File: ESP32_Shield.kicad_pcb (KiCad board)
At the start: 4 copper layers, 69 x 40.6 mm, 36 parts, among them J1 BME280, SHT40 Module, J10 SCD40 Module, J11 Conn_01x03, J12 Conn_01x03, J13 SCD40 Module, J14 BME280, SHT40 Module, J2 SCD40 Module, J3 Conn_01x02, J4 Qwiic_Vertical, J5 Conn_01x02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

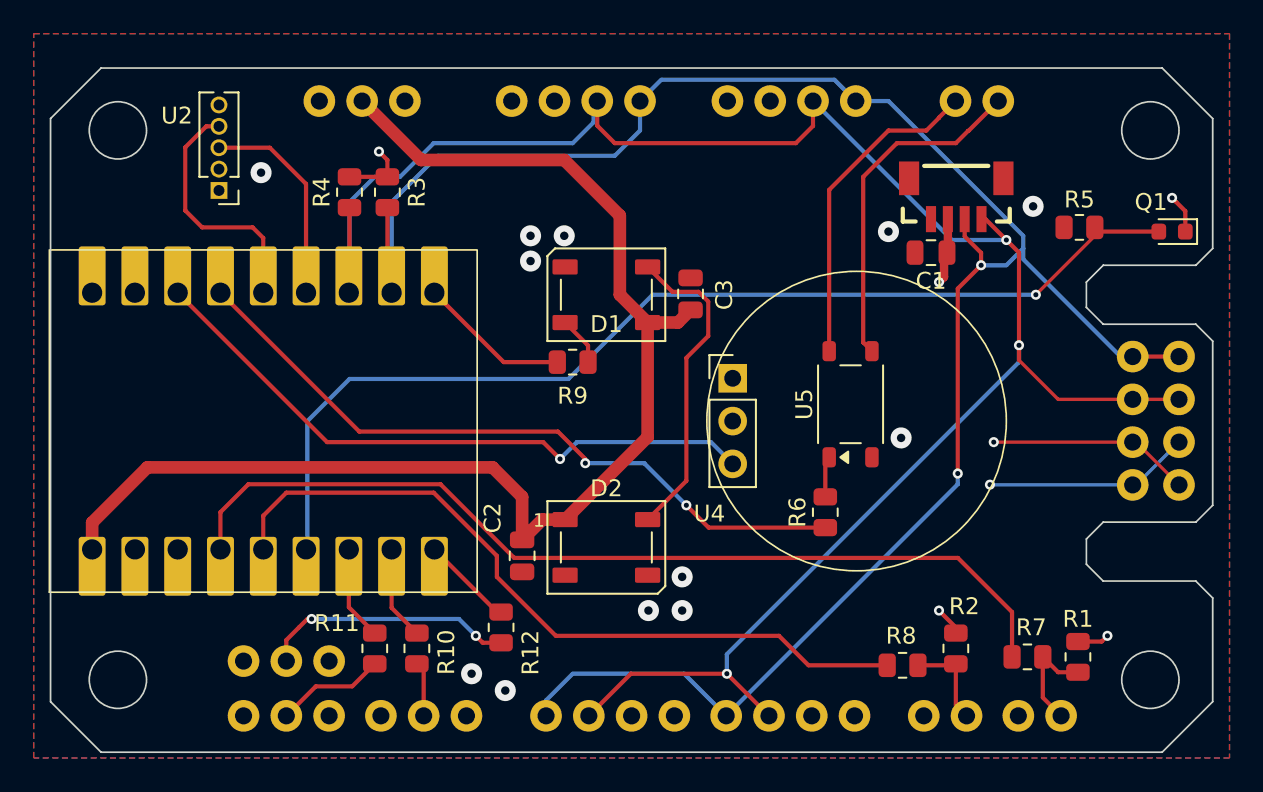
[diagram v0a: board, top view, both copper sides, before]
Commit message: Feature/description on soldermask (#2)
* fix Readme

* enhance README with KiBOT usage instructions and asset generation workflow

* make shure everithing is english

* improve readme

* fix upload path

* fix tittle in readme

* add silk screen and mmWave connector

* Update artifact name in fabrication workflow

* try other pr pipeline

* add more JST connectors for UART

* add jst connector for aditional gpios
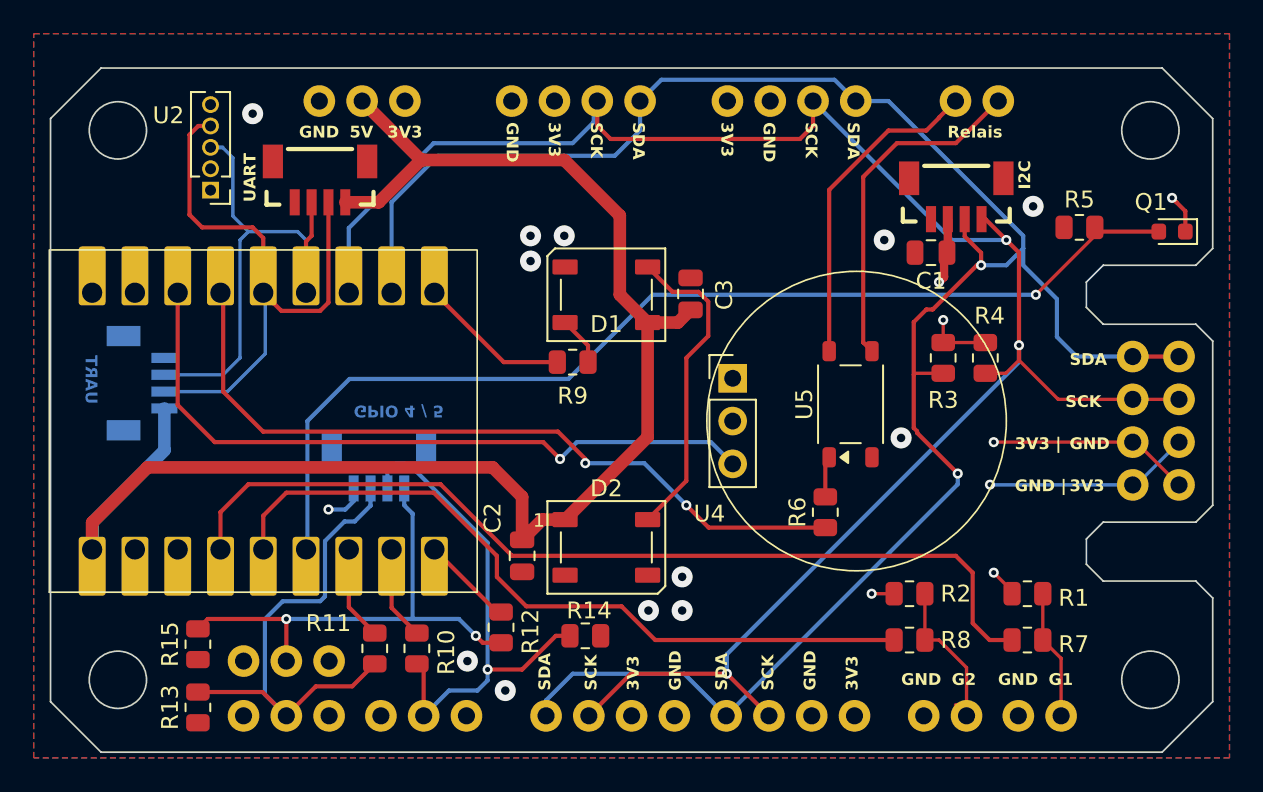
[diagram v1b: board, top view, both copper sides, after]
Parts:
- added J15: mmWave Connector, PCM_SparkFun-Connector:JST_1x04_P1.0mm_Vertical_SMD, B.Cu at (96.2, 86.2)
- added J16: mmWave Connector, PCM_SparkFun-Connector:JST_1x04_P1.0mm_Vertical_SMD, F.Cu at (107.0, 74.0)
- added J17: mmWave Connector, PCM_SparkFun-Connector:JST_1x04_P1.0mm_Vertical_SMD, B.Cu at (110.5, 91.0)
- added R13: 2k2, Resistor_SMD:R_0805_2012Metric, F.Cu at (99.8, 105.5)
- added R14: 2k2, Resistor_SMD:R_0805_2012Metric, F.Cu at (122.8, 101.2)
- added R15: 2k2, Resistor_SMD:R_0805_2012Metric, F.Cu at (99.8, 101.8)
- moved R4 39.0 mm to (146.5, 84.8)
- moved R3 34.4 mm to (144.0, 84.8)
- moved R1 4.80 mm to (149.0, 98.8), turned to 180 degrees
- moved R2 4.26 mm to (142.0, 98.8), turned to 180 degrees
- moved R8 1.56 mm to (142.0, 101.5)
- moved R7 1.00 mm to (149.0, 101.5)
- moved U2 0.50 mm to (100.5, 72.2)
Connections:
- net Net-(J12-Pin_2) renamed GPIO_6_
- net Net-(J7-Pin_2) renamed GPIO_4_
- net Net-(J8-Pin_2) renamed GPIO_5_
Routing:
- net GPIO_5_: track 3.26 -> 30.9 mm, vias 0 -> 1
- net GPIO_4_: track 6.53 -> 30.6 mm
- net UART_TX_mmWAVE: track 14.8 -> 35.5 mm
- net UART_RX_mmWAVE: track 12.5 -> 31.2 mm
- net +5V: track 76.5 -> 92.5 mm
- net GPIO_6_: track 15.1 -> 29.3 mm
- net Net-(J5-Pin_2): track 5.64 -> 9.66 mm
- net PIR: track 38.0 -> 41.9 mm
- net SCK: track 119.2 -> 115.5 mm
- net Relais: track 41.8 -> 45.2 mm
- net +3V3: track 25.9 -> 27.7 mm, vias 6 -> 7
- net Net-(J6-Pin_2): track 6.42 -> 7.70 mm
- net SDA: track 121.3 -> 122.4 mm
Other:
- board text added: "3V3"
- board text added: "3V3 |"
- board text added: "5V"
- board text added: "G1"
- board text added: "G2"
- board text added: "GND"
- board text added: "GND |"
- board text added: "GPIO 4 / 5"
- board text added: "I2C"
- board text added: "Relais"
- board text added: "SCK"
- board text added: "SDA"
- board text added: "UART"
